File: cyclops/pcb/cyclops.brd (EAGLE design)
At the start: 124.5 x 79.9 mm, 169 parts, among them Q2 IRF510, U1 MCP4921, U10 TLV2374, U11 THS4281, U12 MAX4564, U13 ZXTD, U14 ZXTD, U3 MAX4564, U4 LT1931, U5 LT1764A, U6 337L, U67 ZLDO1117, U69 LT1716, U7 TLV3701, U8 ADR03, U9 OP1177

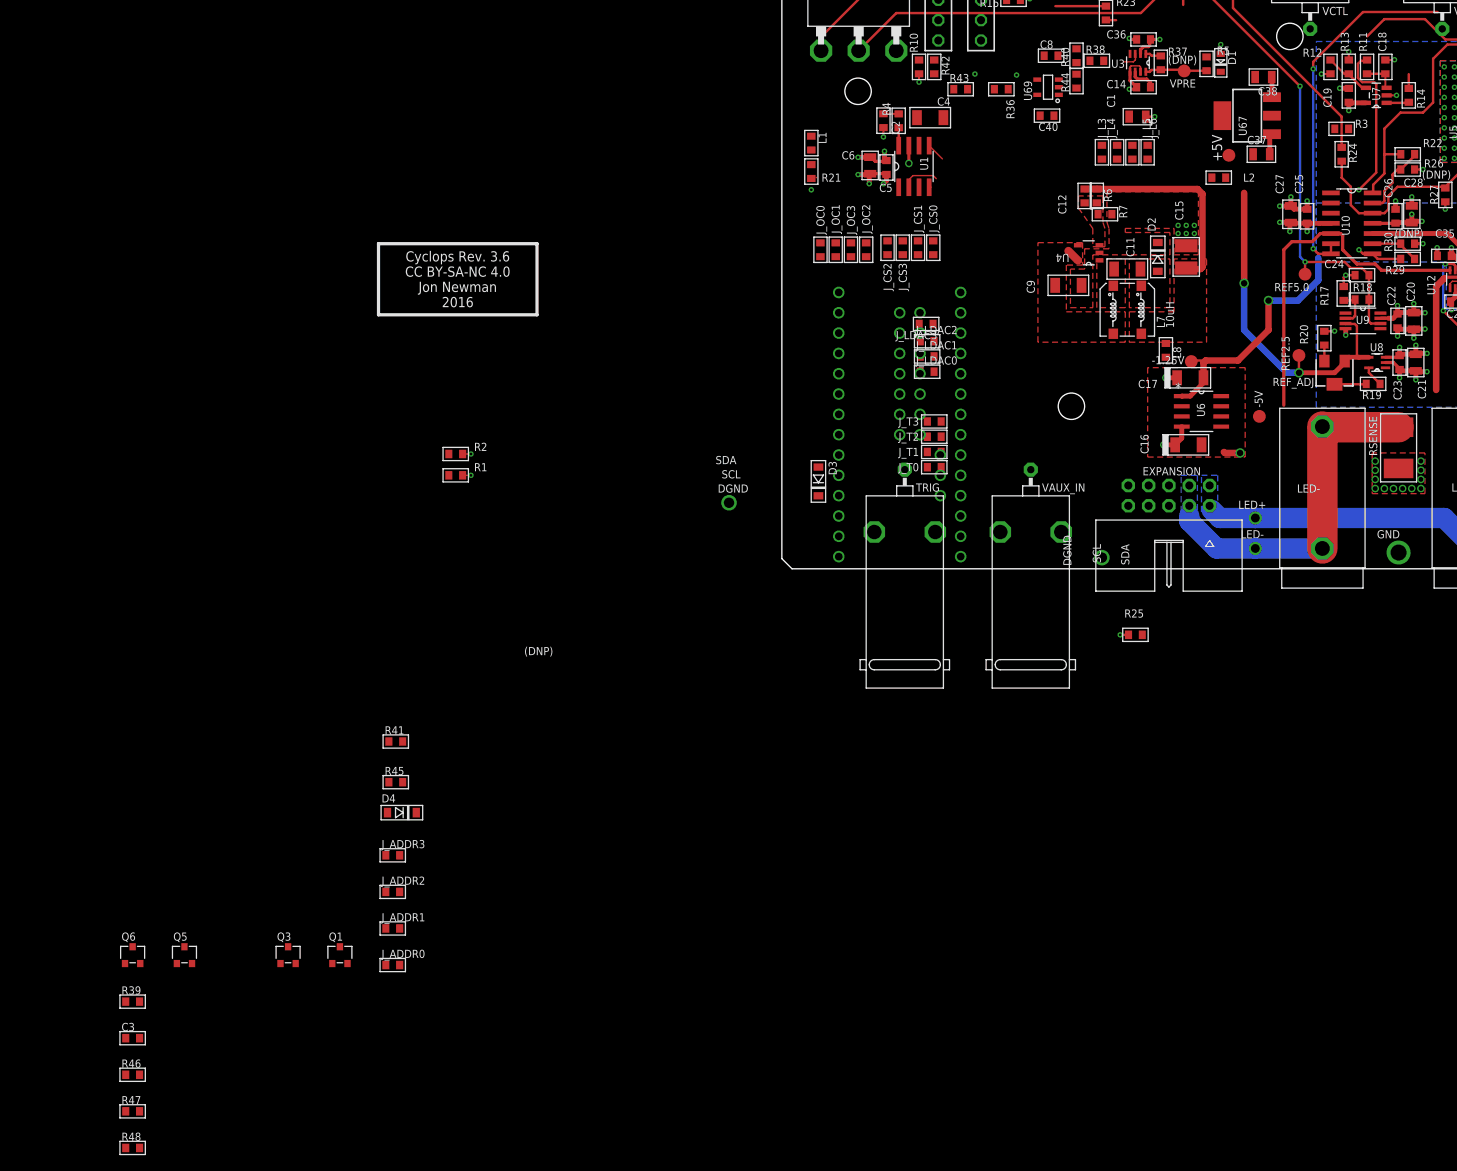
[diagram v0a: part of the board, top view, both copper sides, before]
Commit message: Lots of minor circuit mods
- Replace OC SPDT with a SPST with better bandwidth and larger voltage
  rail capabilities since id does not need the other terminal
- Spice modeling of input circuitry
- Etc
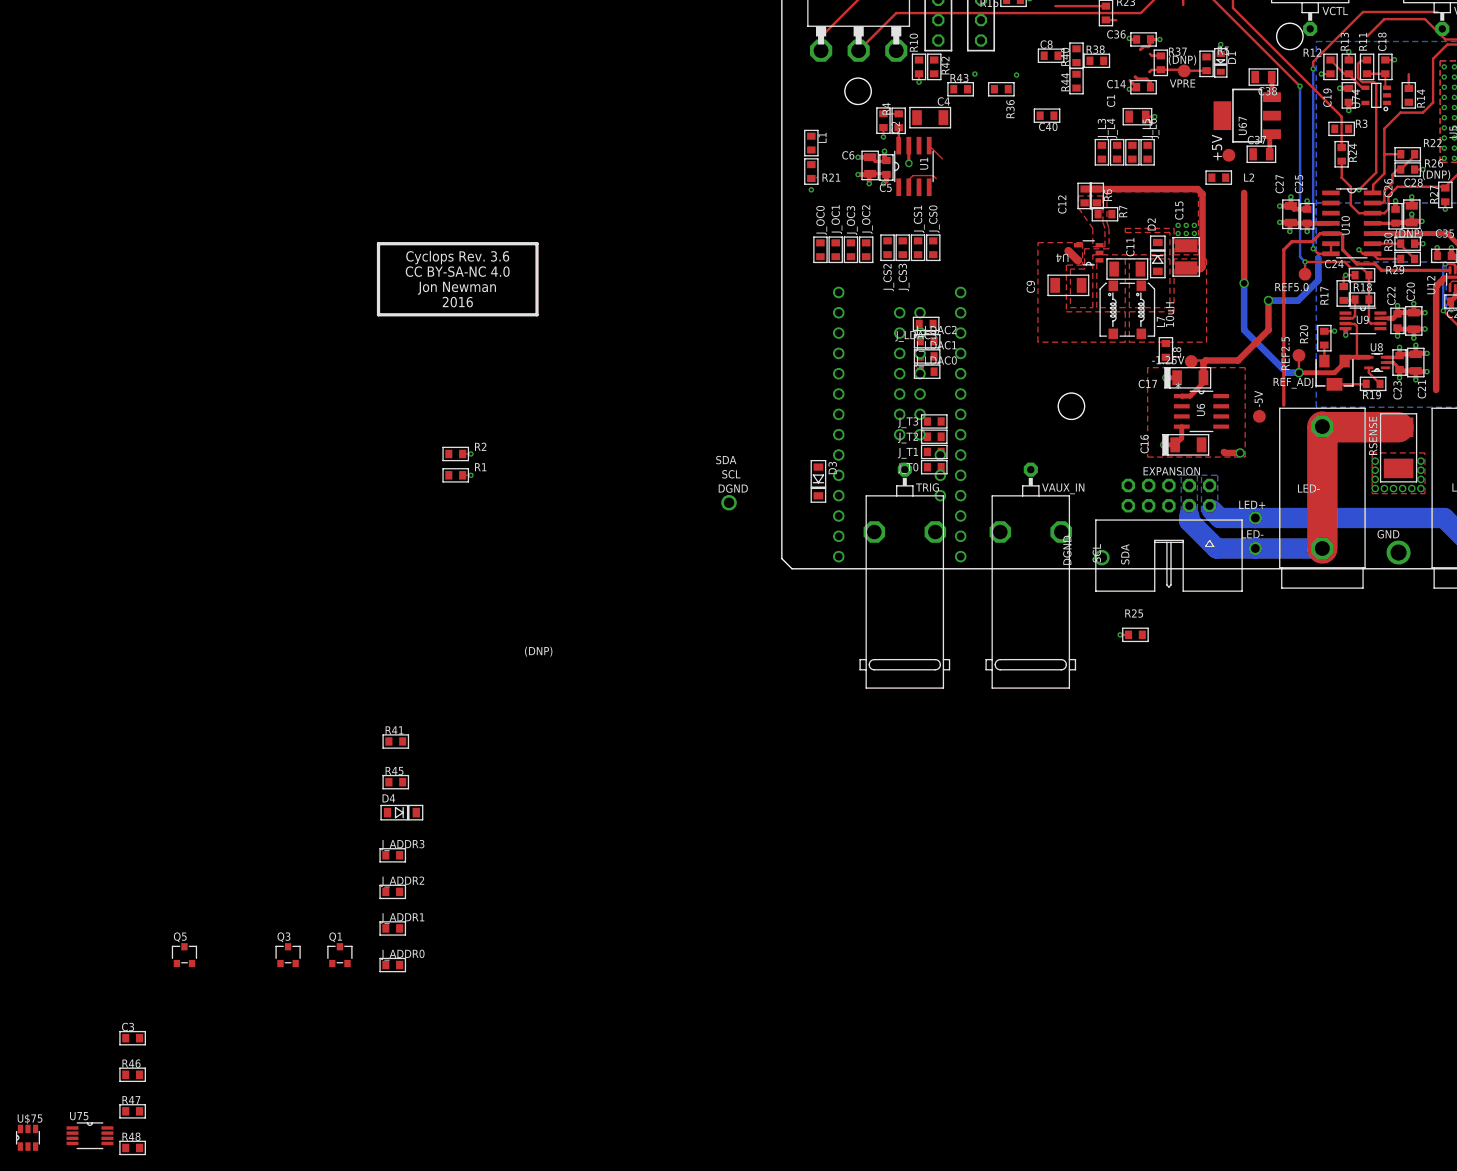
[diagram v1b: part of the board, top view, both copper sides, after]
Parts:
- removed Q6: (no value), jonnew:SOT23-GSD
- removed R39: 1k, cyclops:0603
- removed U3: MAX4564, cyclops:SOT65P300X175-N
- removed U69: LT1716, jonnew:SOT-23-5
- removed U7: TLV3701, ti-extended:SOT95P280X145-5N
- added U$75: (no value), jonnew:SOT23-6
- added U74: TLV3701, jonnew:SOT-23-5
- added U75: LT1711, jonnew:SOP65P490X110-8N
- C14, C36: value 10nF -> 0.1uF
- U10: value TLV2374 -> OPA1664
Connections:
- removed net ~LED_ACTIVE: R38.2, R43.2, U69.1
- new net N$50: R38.2, U75.7
- new net V-: R13.2, U74.2
- net +12V: now also U74.5; no longer C35.1, C36.1, U12.2, U3.2, U7.5
- net +5V: now also C35.1, C36.1, U$75.1, U12.2, U75.1; no longer R39.2, R40.2, U69.5
- net -1.25V: now also U$75.3, U75.4; no longer U3.6, U69.2
- net COMP+: now also U74.3; no longer U7.3
- net GND: now also U$75.2, U75.5, U75.6; no longer Q6.D, R13.2, U3.5, U3.7, U7.2
- net LED_ACTIVE: now also R43.2, U75.8; no longer Q5.D, R39.1
- net N$27: now also U74.1; no longer U7.1
- net N$42: now also U75.2; no longer U69.3
- net N$47: now also Q5.D; no longer Q6.S
- net N$49: no longer Q6.G
- net N$5: now also U74.4; no longer U7.4
- net OVER_CURR: no longer U3.3
- net REF5.0: now also R40.2
- net VCTL: now also U$75.4; no longer U3.8
- net VCTL_PROT: now also U$75.5; no longer U3.1
- net VI_INTERNAL: now also U75.3; no longer U69.4
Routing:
- net +12V: track 60.9 -> 51.5 mm, vias 221 -> 219
- net +5V: track 4.97 -> 11.8 mm, vias 2 -> 4
- net GND: track 74.8 -> 68.7 mm, vias 134 -> 132
- net N$27: track 2.80 -> 0.11 mm
- net OVER_CURR: track 2.41 -> 0.00 mm
- net V-: track 0.00 -> 1.04 mm, vias 0 -> 1
- net N$5: track 6.78 -> 5.84 mm
- net -1.25V: track 57.3 -> 56.7 mm
- net VCTL_PROT: track 3.29 -> 2.78 mm

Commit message: More circuit revisions.
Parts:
- removed +5V, -1.25V: TPTP16R, cyclops:TP16R
- removed C40: .1uF, cyclops:0603
- removed J_ADDR0, J_CS0, J_LDAC0, J_T0: 0, cyclops:0603
- removed J_L5, J_L6: MPZ1608, cyclops:0603
- removed Q5: (no value), jonnew:SOT23-GSD
- removed U$75: (no value), jonnew:SOT23-6
- removed U67: ZLDO1117, jonnew:SOT223
- removed U75: LT1711, jonnew:SOP65P490X110-8N
- added +6V, -2.5V: TPTP16R, cyclops:TP16R
- added C39: 10nF, cyclops:0603
- added C7: 100uF, cyclops:153CLV-0807
- added J_ADDR4, J_CS4, J_LDAC4, J_T4, R49: 0, cyclops:0603
- added J_L1, J_L2: MPZ1608, cyclops:0603
- added Q4: IRF510, cyclops:TO-262_01
- added R39, R50: (no value), cyclops:0603
- added R51: 10k, cyclops:0603
- added U15: OPA1664, jonnew:SO14
- added U2: LT1931, cyclops:SOT95P310X175-5N
- added U3: LT1764A, cyclops:5-DDPAK
- C11: value 1uF -> 22uF; device cyclops:1206 -> cyclops:1210
- C12: value 220pF -> 10uF; device cyclops:0603 -> jonnew:1206
- C13: value 100uF -> 10uF; device cyclops:153CLV-0807 -> jonnew:1206
- C14: value 0.1uF -> 10uF; device cyclops:0603 -> jonnew:1206
- C15: value 22uF -> 10nF; device cyclops:1210 -> cyclops:1206
- C16: value 1uF -> 10uF; device cyclops:1206-POL -> jonnew:1206
- C17: value 1uF -> .1uF; device cyclops:1206-POL -> cyclops:0603
- C20, C21: value 1uF -> .1uF; device cyclops:0805 -> cyclops:0603
- C22, C25, C31, C5: value .1uF -> 1uF; device cyclops:0603 -> cyclops:0805
- C27, C28: value 1uF -> 0.1uF; device cyclops:0805 -> cyclops:0603
- C29, C35: value 10nF -> .1uF
- C3: value .1uF -> 10uF; device cyclops:0603 -> cyclops:1206
- C32: value 220pF -> 1uF; device cyclops:0603 -> cyclops:0805
- C33: value 10uF -> 10nF; device cyclops:1206 -> cyclops:0603
- C34, C4: value 10uF -> .1uF; device cyclops:1206 -> cyclops:0603
- C36: value 0.1uF -> 220pF
- C37, C38: value 1uF -> 10uF; device cyclops:0805 -> cyclops:1206
- C6: value 1uF -> 4.7uF; device cyclops:0805 -> cyclops:1206
- C8: value .1uF -> 1uF; device cyclops:0603 -> cyclops:1206
- C9: value 4.7uF -> 220pF; device cyclops:1206 -> cyclops:0603
- D1: value MM3Z5V1 -> 1N5819; device cyclops:SOD-323 -> jonnew:SOD123
- D2: value MBR0520L -> 1N5819; device cyclops:SOD123 -> jonnew:SOD123
- D3: value 1N5819 -> MM3Z5V1; device jonnew:SOD123 -> cyclops:SOD-323
- D4: value 1N5819 -> MBR0520L; device jonnew:SOD123 -> cyclops:SOD123
- Q2: value IRF510 -> (none); device cyclops:TO-262_01 -> jonnew:SOT23-GSD
- R1: value 10k -> 110k
- R10: value 3k -> 100
- R11: value 10k -> 29.4k
- R12, R3: value 110k -> 10k
- R15: value 1k -> 3k
- R16, R20: value 1k -> 10k
- R17: value 1k -> 40k
- R18, R24: value 1k -> 100k
- R19: value 470 -> 100
- R21: value 110k -> 100k
- R22: value 0 -> 1k
- R23, R28, R32: value 2.2k -> 1k
- R25: value 220k -> 100k
- R26, R30: value (none) -> 1k
- R27: value 220k -> 1k
- R29: value 0 -> 100k
- R31: value 2.2k -> 470
- R33, R34: value 0.5 -> 1k
- R35: value 10k -> 220k
- R36, R43: value 1k -> 0
- R38, R46: value 100k -> 2.2k
- R4: value (none) -> 50; device cyclops:0603 -> jonnew:1206
- R40: value 100k -> 1k
- R41: value 0 -> 220k
- R42: value 1k -> 2.2k
- R44: value 100 -> (none)
- R45: value (none) -> 2.2k
- R47, R48: value 100k -> 0.5
- R5: value 100 -> 50; device cyclops:0603 -> jonnew:1206
- R6: value 29.4k -> 50; device cyclops:0603 -> jonnew:1206
- R7: value 10k -> 50; device cyclops:0603 -> jonnew:1206
- R8: value 2.15k -> 110k
- R9: value 240 -> (none)
- U10: value OPA1664 -> (none); device cyclops:SO14 -> jonnew:SOT23-6
- U11: device cyclops:SOT95P310X175-5N -> jonnew:SOT95P310X175-5N
- U4: value LT1931 -> BD60HC5WEFJ; device cyclops:SOT95P310X175-5N -> jonnew:SOIC127P600X175-9N
- U5: value LT1764A -> TPS72325; device cyclops:5-DDPAK -> jonnew:SOT-23-5
- U6: value 337L -> LT1711; device cyclops:SOIC127P600X175-8N -> jonnew:SOP65P490X110-8N
- U9: value OP1177 -> LT1880; device cyclops:SOP65P490X110-8N -> jonnew:SOT95P310X175-5N
- moved R46 201.9 mm to (91.7, 41.1)
- moved R48 200.6 mm to (87.4, 36.3), turned to 270 degrees
- moved R47 199.8 mm to (89.4, 36.3), turned to 270 degrees
- moved C13 195.8 mm to (-54.1, -48.3), turned to 0 degrees
- moved U9 177.1 mm to (-61.0, -85.3)
- moved U5 173.5 mm to (-55.1, -35.3), turned to 0 degrees
- moved R5 173.0 mm to (-54.1, -72.6), turned to 0 degrees
- moved R45 157.8 mm to (91.7, 46.2), turned to 180 degrees
- moved R7 155.2 mm to (-54.1, -78.7), turned to 0 degrees
- moved U4 152.5 mm to (-61.0, -76.2), turned to 0 degrees
- moved C3 151.9 mm to (18.5, 55.9), turned to 180 degrees
- moved R41 147.9 mm to (82.9, 46.7), turned to 90 degrees
- moved R6 146.8 mm to (-54.1, -66.5), turned to 0 degrees
- moved Q3 143.2 mm to (28.4, 64.0)
- moved Q1 137.1 mm to (24.9, 64.0)
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- renumbered J_OC0 to J_OC4, L7 to L3, L8 to L4, REF2.5 to REF2.1, REF5.0 to REF5.1, U74 to U7
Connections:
- removed net +12V: AUX<FB>CURR.3, C13.+, C19.1, C20.1, C21.1, C22.1, C23.1, C25.1, C27.1, C30.1, C34.1, C38.1, EXPANSION.7, Q2.D, R10.2, R12.1, R15.2, R16.2, R25.2, R31.1, R42.2, R8.2, U10.4, U11.5, U13.1, U14.1, U5.4, U67.3, U7.5, U8.3, U9.7
- removed net +5V: +5V.TP, C35.1, C36.1, C37.1, C5.1, C6.1, C8.1, L2.2, U$75.1, U1.1, U12.2, U67.2, U67.4, U75.1
- removed net -1.25V: -1.25V.TP, C14.1, C17.-, C26.1, C28.1, C29.1, C3.1, C31.1, C33.1, R27.1, R32.2, U$75.3, U10.11, U11.2, U12.6, U13.3, U14.3, U6.1, U75.4
- new net +13.3V: C10.+, C12.1, C34.1, C38.1, EXPANSION.7, Q4.D, R13.2, R15.2, R45.1, U11.5, U13.1, U14.1, U3.4, U4.5, U4.8
- new net +6V: +6V.TP, AUX<FB>CURR.3, C14.1, C19.1, C20.1, C22.1, C23.1, C28.1, C29.1, C31.1, C39.1, C4.1, C5.1, L1.2, R26.2, R27.2, R30.2, R35.2, U1.1, U10.1, U12.2, U15.4, U6.1, U7.5, U8.3
- new net -2.5V: -2.5V.TP, C15.2, C16.2, C21.1, C27.1, C30.1, C32.1, C33.1, C35.1, C37.1, R41.1, R46.2, U10.3, U11.2, U12.6, U13.3, U14.3, U15.11, U5.5, U6.4
- new net N$48: C13.1, C16.1, U5.1
- new net N$51: C15.1, U5.4
- new net N$52: R4.1, VAUX_OUT.1
- new net N$53: R5.1, VAUX_IN.1
- new net N$54: R6.1, VI.1
- new net N$55: R7.1, VREF.1
- new net N$57: C24.2
- new net V+: C24.1, C25.1, U9.5
- net +15V: now also C7.+, U3.1, U3.2; no longer C10.+, U5.1, U5.2
- net +3V3: now also R3.1; no longer R1.1
- net -5V: now also C13.2, U5.2, U5.3; no longer C16.-, U6.2, U6.3, U6.6, U6.7
- net COM: now also C36.1; no longer C32.1
- net COMP+: now also C17.1, R16.1; no longer C18.1, R11.1
- net CS: now also J_CS2.1, J_CS4.2; no longer J_CS0.1, J_CS2.2
- net CS0: now also J_CS2.2; no longer J_CS0.2
- net CS2: now also J_CS3.1; no longer J_CS2.1
- net CS3: now also J_CS4.1; no longer J_CS3.1
- net DACA: now also R9.2; no longer R4.2
- net GND: now also C11.2, C12.2, C17.2, C32.2, C39.2, C7.-, D3.A, D4.C, J_ADDR4.1, Q2.S, R12.1, R14.1, R19.1, R24.1, R25.1, R29.1, R32.1, R33.2, R39.2, R42.2, R44.2, R50.2, R51.1, R8.2, U10.2, U2.2, U3.3, U3.TAB, U4.3, U4.9, U6.5, U6.6; no longer C13.-, C15.2, C16.+, C17.+, C24.2, C36.2, C40.2, C8.2, C9.2, D1.A, D2.C, J_ADDR0.1, Q5.S, R17.2, R20.1, R21.2, R26.2, R28.2, R30.2, R35.1, R44.1, R45.2, R46.1, R47.1, R48.1, R7.1, R9.1, U$75.2, U4.2, U5.3, U5.TAB, U6.4, U67.1, U75.5, U75.6, U9.4
- net LDAC: now also J_LDAC4.2; no longer J_LDAC0.2
- net LDAC0: now also J_LDAC4.1; no longer J_LDAC0.1
- net LDAC1: now also J_LDAC3.2; no longer J_LDAC1.2
- net LDAC3: now also J_LDAC1.2; no longer J_LDAC3.2
- net LED+: now also Q4.S; no longer Q2.S
- net LED-: now also U15.10, U15.3; no longer U10.10, U10.3
- net LED_ACTIVE: now also R23.2, U6.8; no longer R43.2, U75.8
- net N$1: now also R9.1; no longer R4.1
- net N$10: now also R46.1; no longer R32.1
- net N$11: now also R49.1, R50.1, U15.2; no longer R41.1, R45.1, U10.2
- net N$12: now also R13.1, R14.2, U3.5; no longer R8.1, R9.2, U5.5
- net N$13: now also C36.2, R42.1; no longer C32.2, R28.1
- net N$14: now also R10.1; no longer R5.1
- net N$15: now also R43.1, R44.1, U15.9; no longer R29.1, R30.1, U10.9
- net N$16: now also R30.1; no longer R16.1
- net N$18: now also R33.1, R34.2, U9.4; no longer R17.1, R18.2, U9.2
- net N$19: now also J_L3.1; no longer J_L5.1
- net N$2: now also R26.1; no longer R15.1
- net N$20: now also R31.2; no longer R19.2
- net N$21: now also J_L2.1; no longer J_L4.1
- net N$22: now also R31.1; no longer R19.1
- net N$23: now also J_L1.1; no longer J_L3.1
- net N$24: now also R48.1; no longer R34.1
- net N$25: now also R47.1; no longer R33.1
- net N$26: now also Q4.G, R47.2, R48.2, R51.2; no longer Q2.G, R33.2, R34.2, R35.2
- net N$27: now also R22.2; no longer R14.2
- net N$28: now also R22.1, R24.2; no longer R14.1, R47.2
- net N$3: now also R15.1; no longer R10.1
- net N$32: now also C8.1, U2.1; no longer C11.1, U4.1
- net N$33: now also C8.2, D4.A; no longer C11.2, D2.A
- net N$35: now also C11.1, C9.1, R11.2; no longer C12.1, C15.1, R6.2
- net N$36: now also C9.2, R11.1, R12.2, U2.3; no longer C12.2, R6.1, R7.2, U4.3
- net N$37: now also R40.1; no longer R24.1
- net N$38: now also L2.2, R8.1; no longer L1.2, R21.1
- net N$39: now also R28.1, R29.2; no longer R36.1, R48.2
- net N$4: now also R45.2; no longer R31.2
- net N$40: now also J_ADDR1.2; no longer J_ADDR3.2
- net N$42: now also R18.1, R19.2, R21.1, U6.2; no longer R38.1, R40.1, R44.2, U75.2
- net N$43: now also D2.A, L1.1; no longer D3.A, L2.1
- net N$44: now also J_ADDR3.2; no longer J_ADDR1.2
- net N$45: now also J_ADDR4.2; no longer J_ADDR0.2
- net N$46: now also R27.1; no longer R42.1
- net N$47: now also Q2.D; no longer Q5.D
- net N$49: now also Q2.G, R23.1, R25.2; no longer Q5.G, R43.1, R46.2
- net N$5: now also C18.1, R17.2, R20.1; no longer C40.1, R12.2, R13.1
- net N$50: now also R21.2, U6.7; no longer R38.2, U75.7
- net N$6: now also R32.2; no longer R20.2
- net N$7: now also J_L4.1; no longer J_L6.1
- net N$8: now also R36.1, R39.1, U15.13; no longer R22.1, R26.1, U10.13
- net OC1: now also J_OC3.2; no longer J_OC1.2
- net OC3: now also J_OC1.2; no longer J_OC3.2
- net OVER_CURR: now also L2.1, R28.2; no longer L1.1, R36.2
- net REF2.5: now also C3.1; no longer C4.1
- net REF5.0: now also C26.1, R17.1, R18.2, R34.1, U9.1; no longer C24.1, R18.1, R40.2, U9.6
- net SCL: now also R2.2; no longer R1.2
- net SDA: now also R3.2; no longer R2.2
- net T0: now also J_T1.1; no longer J_T0.1
- net T1: now also J_T2.1; no longer J_T1.1
- net T2: now also J_T3.1; no longer J_T2.1
- net T3: now also J_T4.1; no longer J_T3.1
- net TRIG: now also J_T4.2; no longer J_T0.2
- net V-: now also R20.2, U9.2; no longer R13.2
- net VAUX: now also R35.1, R5.2, U15.5; no longer R25.1, U10.5, VAUX_IN.1
- net VAUX_OUT: now also R4.2, U15.6, U15.7; no longer U10.6, U10.7, VAUX_OUT.1
- net VCTL: now also D3.C, R10.2, U10.4; no longer D1.C, R5.2, U$75.4
- net VCTL_PROT: now also R38.2, U10.5; no longer R23.2, U$75.5
- net VCTL_PROTECT: now also R38.1; no longer R23.1
- net VI: now also R43.2, R6.2, U15.8; no longer R29.2, U10.8, VI.1
- net VIN: now also C6.1, D2.C, U2.4, U2.5; no longer C9.1, D3.C, U4.4, U4.5
- net VI_INTERNAL: now also R1.1, R16.2, R49.2, U15.1, U6.3; no longer R11.2, R3.1, R41.2, U10.1, U75.3
- net VI_LP: now also J_L1.2, J_L2.2, R1.2; no longer J_L5.2, J_L6.2, R3.2
- net VREF: now also R36.2, U15.14; no longer R22.2, U10.14
- net VREF/TTL: now also R7.2; no longer VREF.1
- net _VREF: now also R40.2, R41.2, U15.12; no longer R24.2, R27.2, U10.12
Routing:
- net -1.25V: track 56.7 -> 0.00 mm, vias 10 -> 0
- net +12V: track 51.5 -> 0.00 mm, vias 219 -> 0
- net -2.5V: track 0.00 -> 43.0 mm, vias 0 -> 10
- net +6V: track 0.00 -> 25.5 mm, vias 0 -> 9
- net +13.3V: track 0.00 -> 24.8 mm, vias 0 -> 212
- net N$37: track 44.5 -> 21.4 mm
- net VREF: track 46.7 -> 30.4 mm
- net +5V: track 11.8 -> 0.00 mm, vias 4 -> 0
- net GND: track 68.7 -> 58.3 mm, vias 132 -> 128
- net _VREF: track 43.4 -> 37.4 mm
- net VCTL: track 7.37 -> 1.84 mm
- net V+: track 0.00 -> 3.89 mm, vias 0 -> 1
- net N$8: track 9.22 -> 6.90 mm
- net N$28: track 1.79 -> 0.00 mm
- net N$18: track 4.84 -> 3.92 mm
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- added copper zone on layer 1, net +13.3V
- added copper zone on layer 15, net +13.3V
- added copper zone on layer 16, net +13.3V
- added copper zone on layer 16, net -2.5V
- removed copper zone on layer 1, net +12V
- removed copper zone on layer 15, net +12V
- removed copper zone on layer 16, net +12V
- removed copper zone on layer 16, net -1.25V

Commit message: Minor layout.
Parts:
- moved R15 26.2 mm to (5.08, 62.5), turned to 270 degrees
- moved R27 22.5 mm to (7.11, 62.5), turned to 270 degrees
- moved R26 20.5 mm to (10.4, 62.5), turned to 270 degrees
- moved R30 16.8 mm to (12.4, 62.5), turned to 270 degrees
- moved R28 15.3 mm to (14.2, 54.6)
- moved R22 15.2 mm to (10.2, 54.6)
- moved R24 15.2 mm to (10.2, 56.4)
- moved Q1 15.2 mm to (10.2, 60.2)
- moved Q3 14.7 mm to (14.2, 60.2)
- moved R23 14.6 mm to (6.10, 54.6)
- moved R29 14.4 mm to (14.2, 56.4)
- moved Q2 14.0 mm to (6.10, 60.2)
- moved R25 13.6 mm to (6.10, 56.4)
- moved IND 13.5 mm to (6.10, 64.8)
- moved OC 13.5 mm to (11.4, 64.8)
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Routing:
- net VINPUT: track 71.9 -> 5.03 mm
- net N$34: track 41.1 -> 3.89 mm
- net N$9: track 0.00 -> 15.8 mm
- net N$2: track 0.00 -> 9.78 mm
- net N$3: track 0.00 -> 9.63 mm
- net N$47: track 0.00 -> 9.58 mm
- net OC: track 0.00 -> 9.54 mm
- net GND: track 58.3 -> 67.0 mm, vias 128 -> 129
- net N$39: track 0.00 -> 3.65 mm
- net N$49: track 0.00 -> 3.52 mm
- net N$28: track 0.00 -> 3.52 mm
- net N$46: track 0.00 -> 3.11 mm
- net N$16: track 0.00 -> 3.11 mm
